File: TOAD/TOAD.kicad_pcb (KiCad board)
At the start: 2 copper layers, 70 x 75 mm, 142 parts, among them IC1 STM32F405RxTx, IC10 ADP3335, IC11 CS2100-CP, IC12 BGS12AL7, IC13 SL18860DC, IC2 Si4463, IC3 MAX-M8Q, IC4 SN74LVC1G0832, IC5 BGS12AL7, IC6 ADP3335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

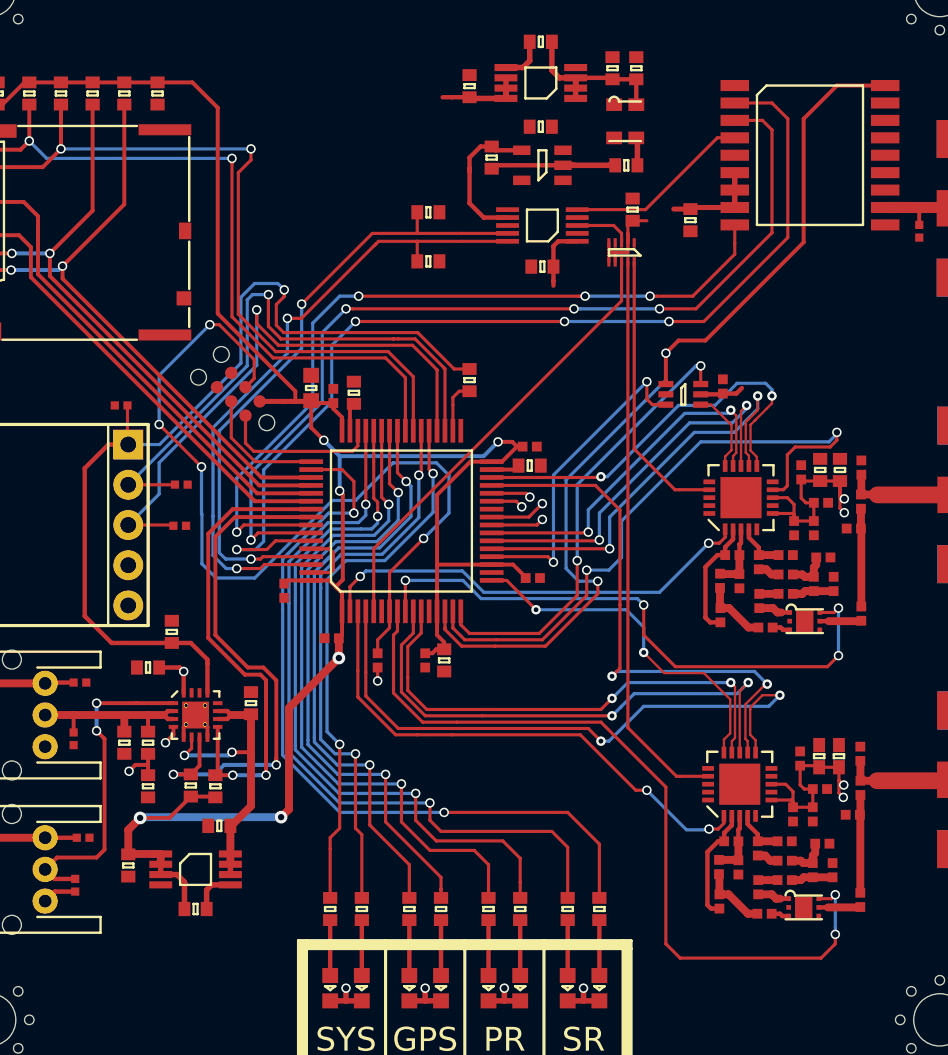
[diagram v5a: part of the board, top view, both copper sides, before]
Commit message: finished all signal and power routing
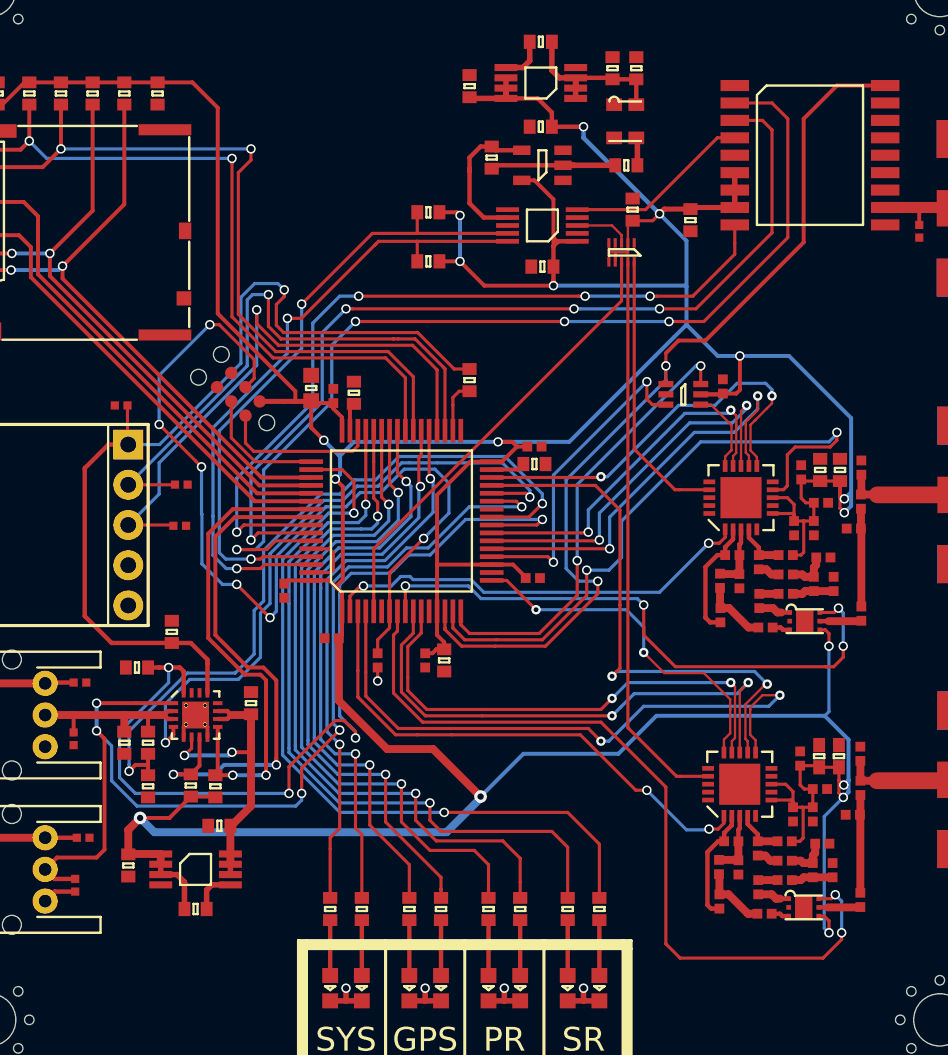
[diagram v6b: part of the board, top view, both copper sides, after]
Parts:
- moved R9 0.70 mm to (69.3, 102.8)
- moved C10 0.32 mm to (94.4, 89.9)
- moved C8 0.30 mm to (94.4, 88.8)
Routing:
- net 3v3: track 199.0 -> 353.0 mm, vias 10 -> 17
- net /I_CHG_MON: track 6.35 -> 59.0 mm, vias 2 -> 4
- net /B_TEMP: track 22.8 -> 67.9 mm, vias 3 -> 5
- net /V_BAT_MON: track 6.27 -> 47.2 mm
- net /CHG_EN: track 3.72 -> 40.2 mm
- net /~RST: track 55.6 -> 59.2 mm, vias 4 -> 6
- net /GPS_PPS: track 59.3 -> 58.6 mm
- net /PR_SDN: track 28.2 -> 27.5 mm

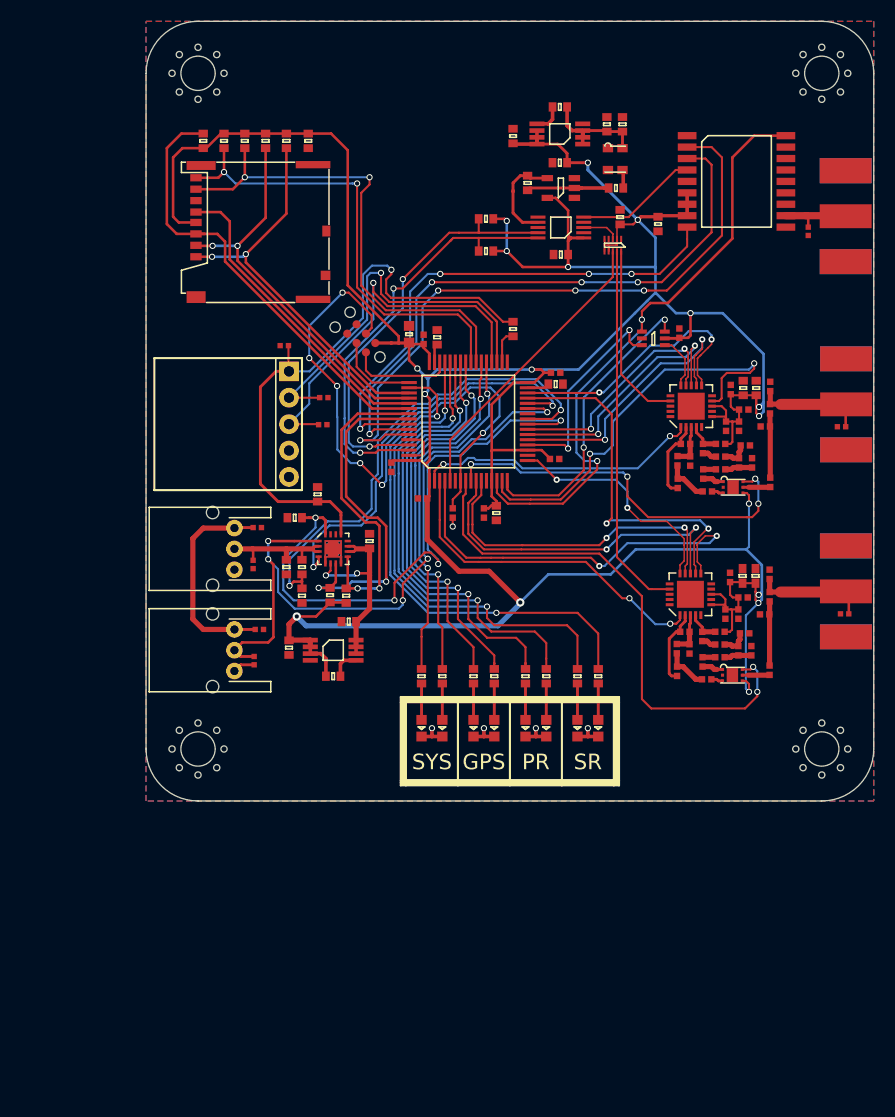
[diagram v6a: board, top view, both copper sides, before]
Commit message: via stitching, silk and test points all still todo
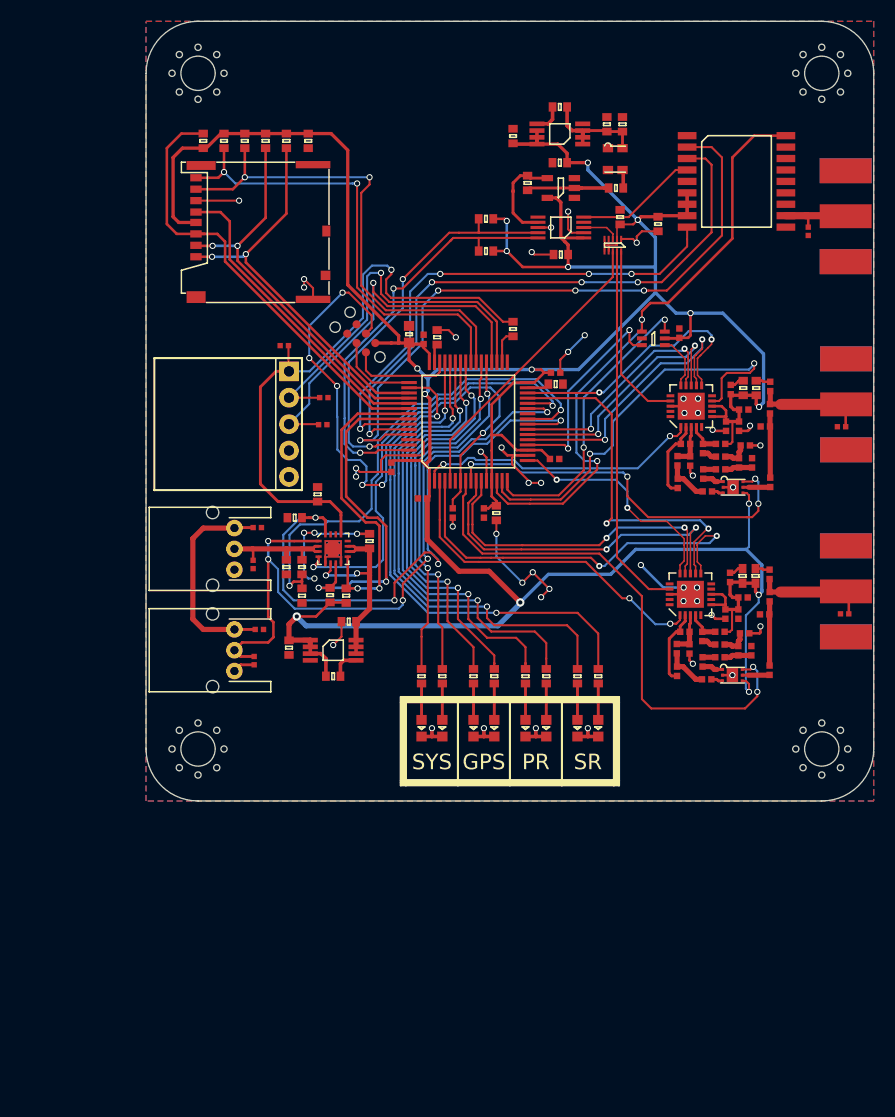
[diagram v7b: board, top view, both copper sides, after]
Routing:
- net GND: track 20.0 -> 127.9 mm, vias 5 -> 49
- net 3v3: track 353.0 -> 359.0 mm, vias 17 -> 15
- net /CHG_EN: track 40.2 -> 42.5 mm
- net /~RST: track 59.2 -> 60.8 mm
- net /V_BAT_MON: track 47.2 -> 48.5 mm
- net /I_CHG_MON: track 59.0 -> 59.8 mm

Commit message: finished via stitching
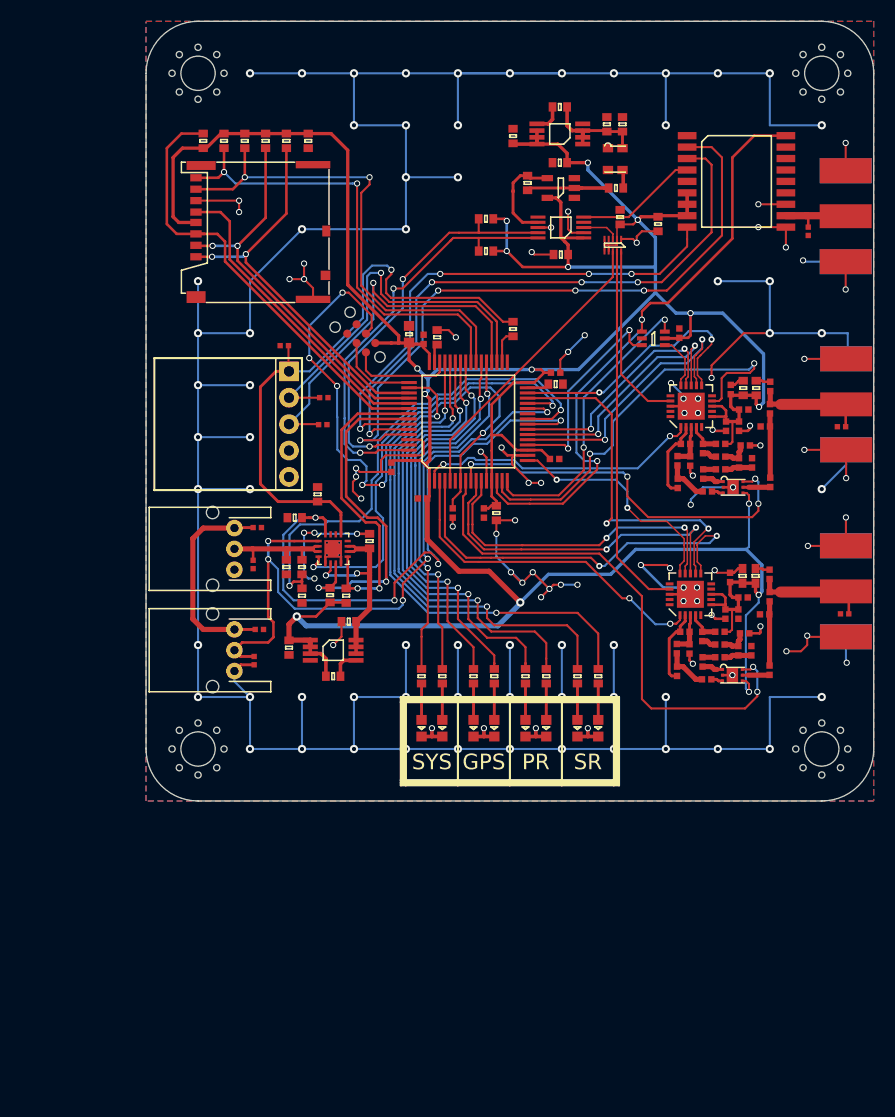
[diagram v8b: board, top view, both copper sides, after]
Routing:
- net GND: track 127.9 -> 552.9 mm, vias 49 -> 137
